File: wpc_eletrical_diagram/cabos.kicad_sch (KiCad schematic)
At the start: 3 parts

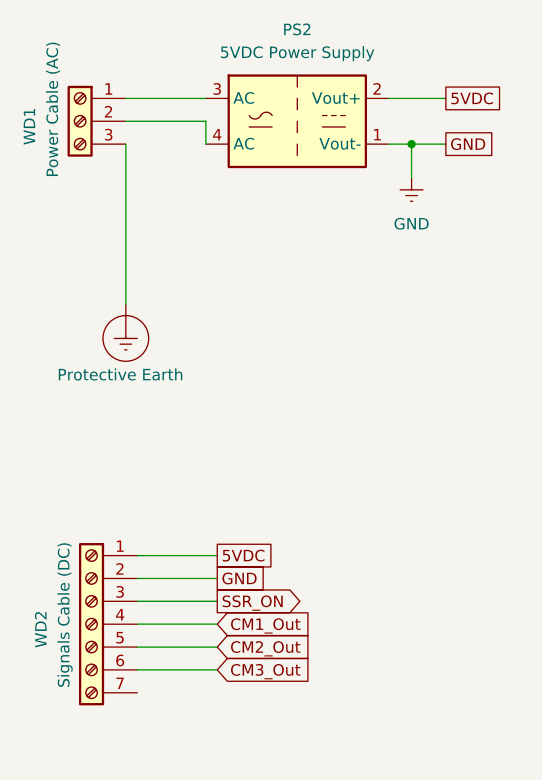
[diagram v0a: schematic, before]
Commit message: eletrical corrections
- schematic correction (sensors, actuation)
- main board correction (resistor values, chottky diodes) (v26)
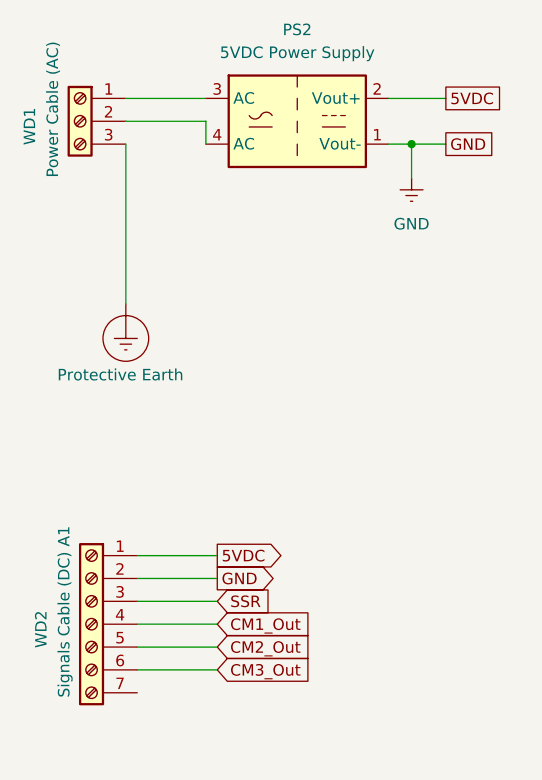
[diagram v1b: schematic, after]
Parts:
- WD2: value Signals Cable (DC) -> Signals Cable (DC) A1
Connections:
- net SSR_ON renamed SSR
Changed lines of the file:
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@@
 	)
 	(global_label "GND"
-		(shape passive)
+		(shape output)
 		(at 49.53 86.36 0)
 		(fields_autoplaced yes)
@@
 		)
 		(property "Intersheetrefs" "${INTERSHEET_REFS}"
-			(at 55.2744 86.36 0)
+			(at 56.3857 86.36 0)
 			(effects
 				(font
@@
 		)
 	)
-	(global_label "SSR_ON"
+	(global_label "SSR"
+		(shape input)
+		(at 49.53 88.9 0)
+		(fields_autoplaced yes)
+		(effects
+			(font
+				(size 1.27 1.27)
+			)
+			(justify left)
+		)
+		(property "Intersheetrefs" "${INTERSHEET_REFS}"
+			(at 56.2042 88.9 0)
+			(effects
+				(font
+					(size 1.27 1.27)
+				)
+				(justify left)
+			)
+		)
+	)
+	(global_label "5VDC"
 		(shape output)
-		(at 49.53 88.9 0)
-		(fields_autoplaced yes)
-		(effects
-			(font
-				(size 1.27 1.27)
-			)
-			(justify left)
-		)
-		(property "Intersheetrefs" "${INTERSHEET_REFS}"
-			(at 59.8328 88.9 0)
-			(effects
-				(font
-					(size 1.27 1.27)
-				)
-				(justify left)
-			)
-		)
-	)
-	(global_label "5VDC"
-		(shape passive)
 		(at 49.53 83.82 0)
 		(fields_autoplaced yes)
@@
 		)
 		(property "Intersheetrefs" "${INTERSHEET_REFS}"
-			(at 56.242 83.82 0)
+			(at 57.3533 83.82 0)
 			(effects
 				(font
@@
 			)
 		)
-		(property "Value" "Signals Cable (DC)"
-			(at 32.512 82.296 90)
-			(effects
-				(font
+		(property "Value" "Signals Cable (DC) A1"
+			(at 32.512 80.518 90)
+			(effects
+				(font
